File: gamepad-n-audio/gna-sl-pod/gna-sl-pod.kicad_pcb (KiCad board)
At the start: 2 copper layers, 29 x 72 mm, 13 parts, among them J1 Gamepad, J2 Gamepad, J3 Gamepads, J4 Gamepad, J5 Gamepad

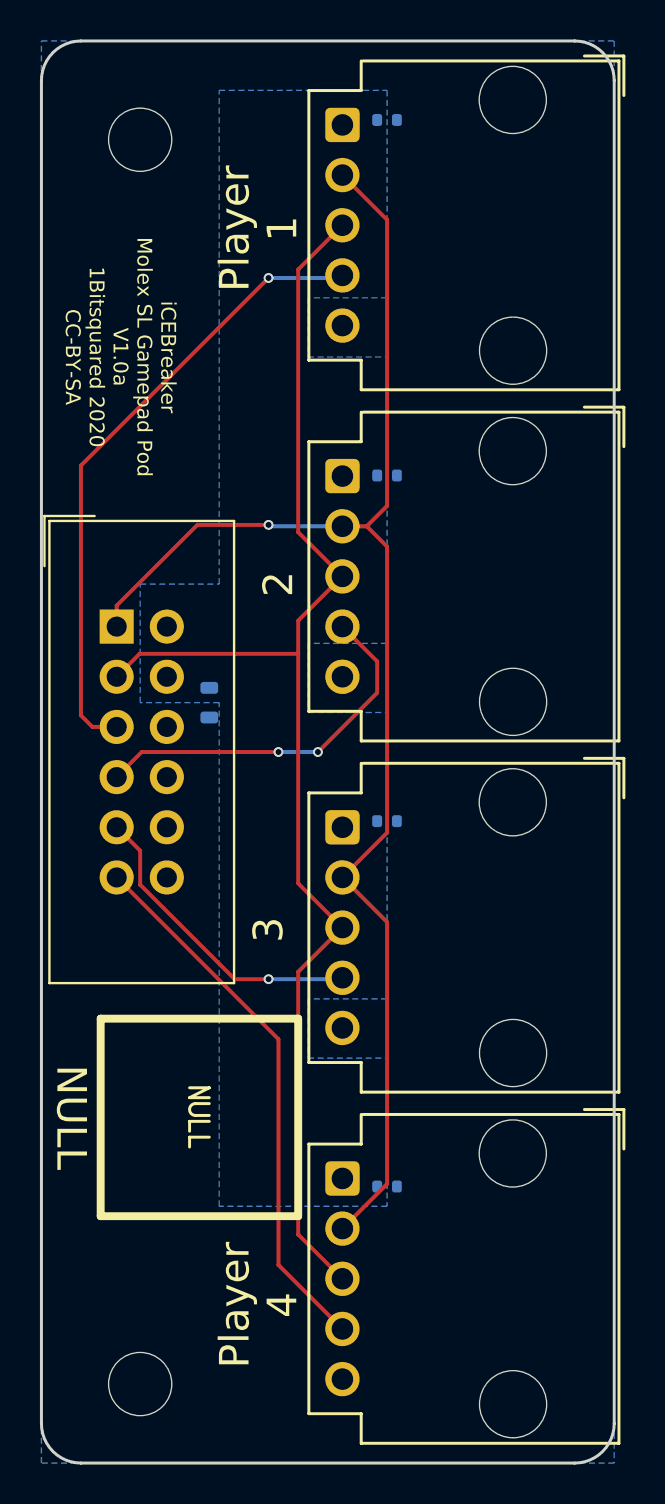
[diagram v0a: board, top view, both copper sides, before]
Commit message: gna SL pod: Removed GND fill on the back and replaced with chonky bus.
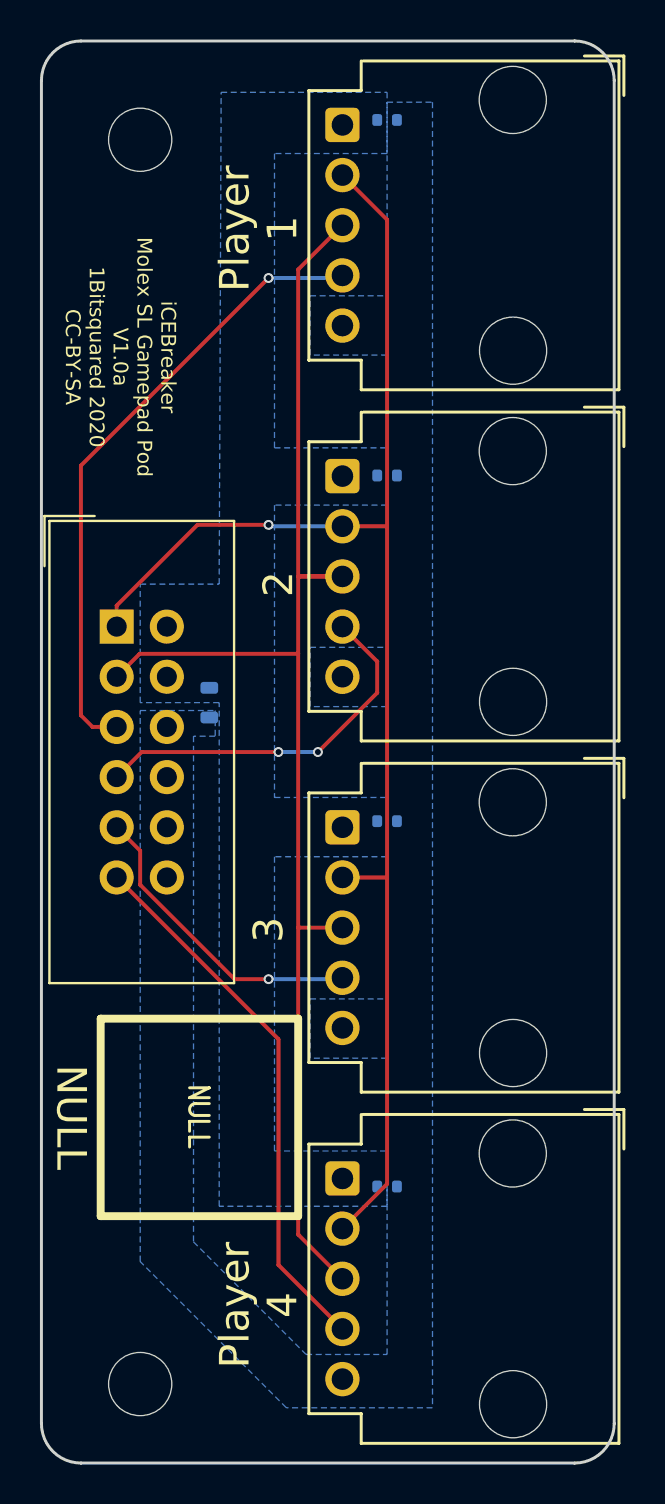
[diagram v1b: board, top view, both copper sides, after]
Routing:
- net /LATCH: track 68.6 -> 71.6 mm
- net /CLK: track 73.4 -> 73.9 mm

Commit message: gna SL/SNES pod: Bumped version.
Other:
- board text added: "iCEBreaker Molex SL Gamepad Pod V1.0b 1Bitsquared 2020 CC-BY-SA"
- board text removed: "iCEBreaker Molex SL Gamepad Pod V1.0a 1Bitsquared 2020 CC-BY-SA"
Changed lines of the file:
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@@
   (title_block
     (title "iCEBreaker PMOD - Gamepad & Audio - Molex SL Pod")
-    (rev V1.0a)
+    (rev V1.0b)
     (company 1BitSquared)
     (comment 1 "2020 (C) 1BitSquared <info@1bitsquared.com>")
@@
     )
   )
-  (gr_text "iCEBreaker\nMolex SL Gamepad Pod\nV1.0a\n1Bitsquared 2020\nCC-BY-SA" (at 41.4 54 270) (layer B.SilkS)
+  (gr_text "iCEBreaker\nMolex SL Gamepad Pod\nV1.0b\n1Bitsquared 2020\nCC-BY-SA" (at 41.4 54 270) (layer B.SilkS)
     (effects (font (size 0.75 0.75) (thickness 0.1875)) (justify mirror))
   )
@@
     (effects (font (size 1.5 1.5) (thickness 0.375)))
   )
-  (gr_text "iCEBreaker\nMolex SL Gamepad Pod\nV1.0a\n1Bitsquared 2020\nCC-BY-SA" (at 41.4 54 270) (layer F.SilkS)
+  (gr_text "iCEBreaker\nMolex SL Gamepad Pod\nV1.0b\n1Bitsquared 2020\nCC-BY-SA" (at 41.4 54 270) (layer F.SilkS)
     (effects (font (size 0.75 0.75) (thickness 0.1875)))
   )
